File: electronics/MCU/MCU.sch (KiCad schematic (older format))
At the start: 34 parts, among them J1 UART, J11 Button, J12 Power, J2 Relay +5V, J3 Conn_01x09, J4 GND, Q1 IRLML 2502, Q10 IRLML 2502, Q2 BSS138, Q3 IRLML 2502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

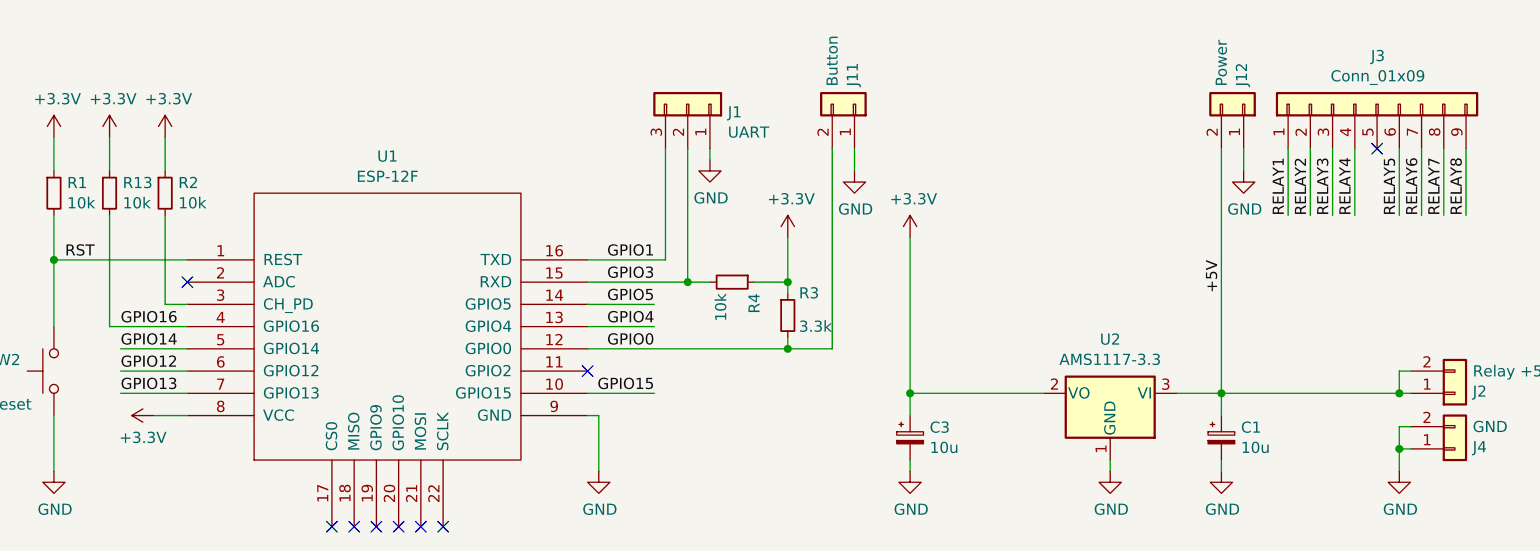
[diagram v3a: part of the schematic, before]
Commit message: MCU: removed pullup from CH_PD (direct 3.3V)      improved clearance around the antenna added FreeCad design for case (uncompressed)
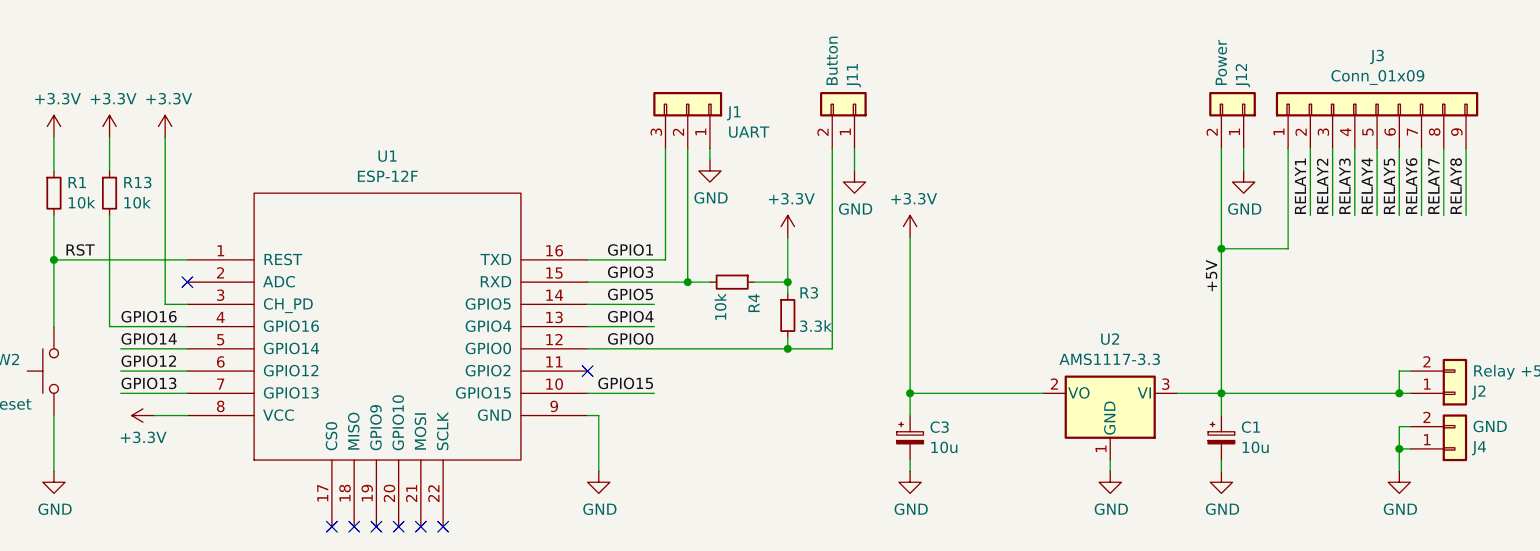
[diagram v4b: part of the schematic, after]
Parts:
- removed R2: 10k, Resistor_SMD:R_0603_1608Metric_Pad1.05x0.95mm_HandSolder, symbol Device:R_Small
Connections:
- net +3V3: now also U1.3 (CH_PD)
- net +5V: now also J3.1 (Pin_1)
- net RELAY1: now also J3.2 (Pin_2); no longer J3.1 (Pin_1)
- net RELAY2: now also J3.3 (Pin_3); no longer J3.2 (Pin_2)
- net RELAY3: now also J3.4 (Pin_4); no longer J3.3 (Pin_3)
- net RELAY4: now also J3.5 (Pin_5); no longer J3.4 (Pin_4)
- no-connect marks 9 -> 8
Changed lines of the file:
@@
 	1    0    0    -1
 $EndComp
-Wire Wire Line
-	3300 1900 3300 2050
 $Comp
 L power:+3.3V #PWR0112
@@
 $EndComp
 Wire Wire Line
-	3300 2250 3300 2650
-$Comp
-L Device:R_Small R2
-U 1 1 607EFCB4
-P 3300 2150
-F 0 "R2" H 3359 2196 50  0000 L CNN
-F 1 "10k" H 3359 2105 50  0000 L CNN
-F 2 "Resistor_SMD:R_0603_1608Metric_Pad1.05x0.95mm_HandSolder" H 3300 2150 50  0001 C CNN
-F 3 "~" H 3300 2150 50  0001 C CNN
-	1    3300 2150
-	1    0    0    -1
-$EndComp
+	3300 1900 3300 2650
 $Comp
 L Connector_Generic:Conn_01x02 J11
@@
 Wire Wire Line
 	9150 1950 9150 2250
-Text Label 8350 2250 1    50   ~ 0
+Text Label 8450 2250 1    50   ~ 0
 RELAY1
-Text Label 8450 2250 1    50   ~ 0
+Text Label 8550 2250 1    50   ~ 0
 RELAY2
-Text Label 8550 2250 1    50   ~ 0
+Text Label 8650 2250 1    50   ~ 0
 RELAY3
-Text Label 8650 2250 1    50   ~ 0
+Text Label 8750 2250 1    50   ~ 0
 RELAY4
 Text Label 8850 2250 1    50   ~ 0
@@
 $EndComp
 Wire Wire Line
-	8050 1950 8050 3050
-Wire Wire Line
-	8350 1950 8350 2250
-NoConn ~ 8750 1950
+	8050 1950 8050 2400
+Wire Wire Line
+	8350 1950 8350 2400
 $Comp
 L Connector_Generic:Conn_01x02 J2
@@
 	8050 3050 8850 3050
 Connection ~ 8850 3050
+Wire Wire Line
+	8750 1950 8750 2250
+Wire Wire Line
+	8350 2400 8050 2400
+Connection ~ 8050 2400
+Wire Wire Line
+	8050 2400 8050 3050
 $EndSCHEMATC
